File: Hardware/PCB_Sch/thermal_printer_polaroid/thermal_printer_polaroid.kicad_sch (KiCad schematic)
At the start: 45 parts, among them J2 USB4085-GF-A, SW0 SW_UP, SW1 SW_CAPTURE, SW2 SW_LEFT, SW3 SW_RIGHT, SW4 SW_DOWN, U1 TM4C123GH6PMI, U2 ov7670_module, U3 thermal_printer, U4 ST7735_LCD, U5 ESP8266_BREAKOUT, U6 UCC381DP-5G4, Y1 8 pF, 16 MHz

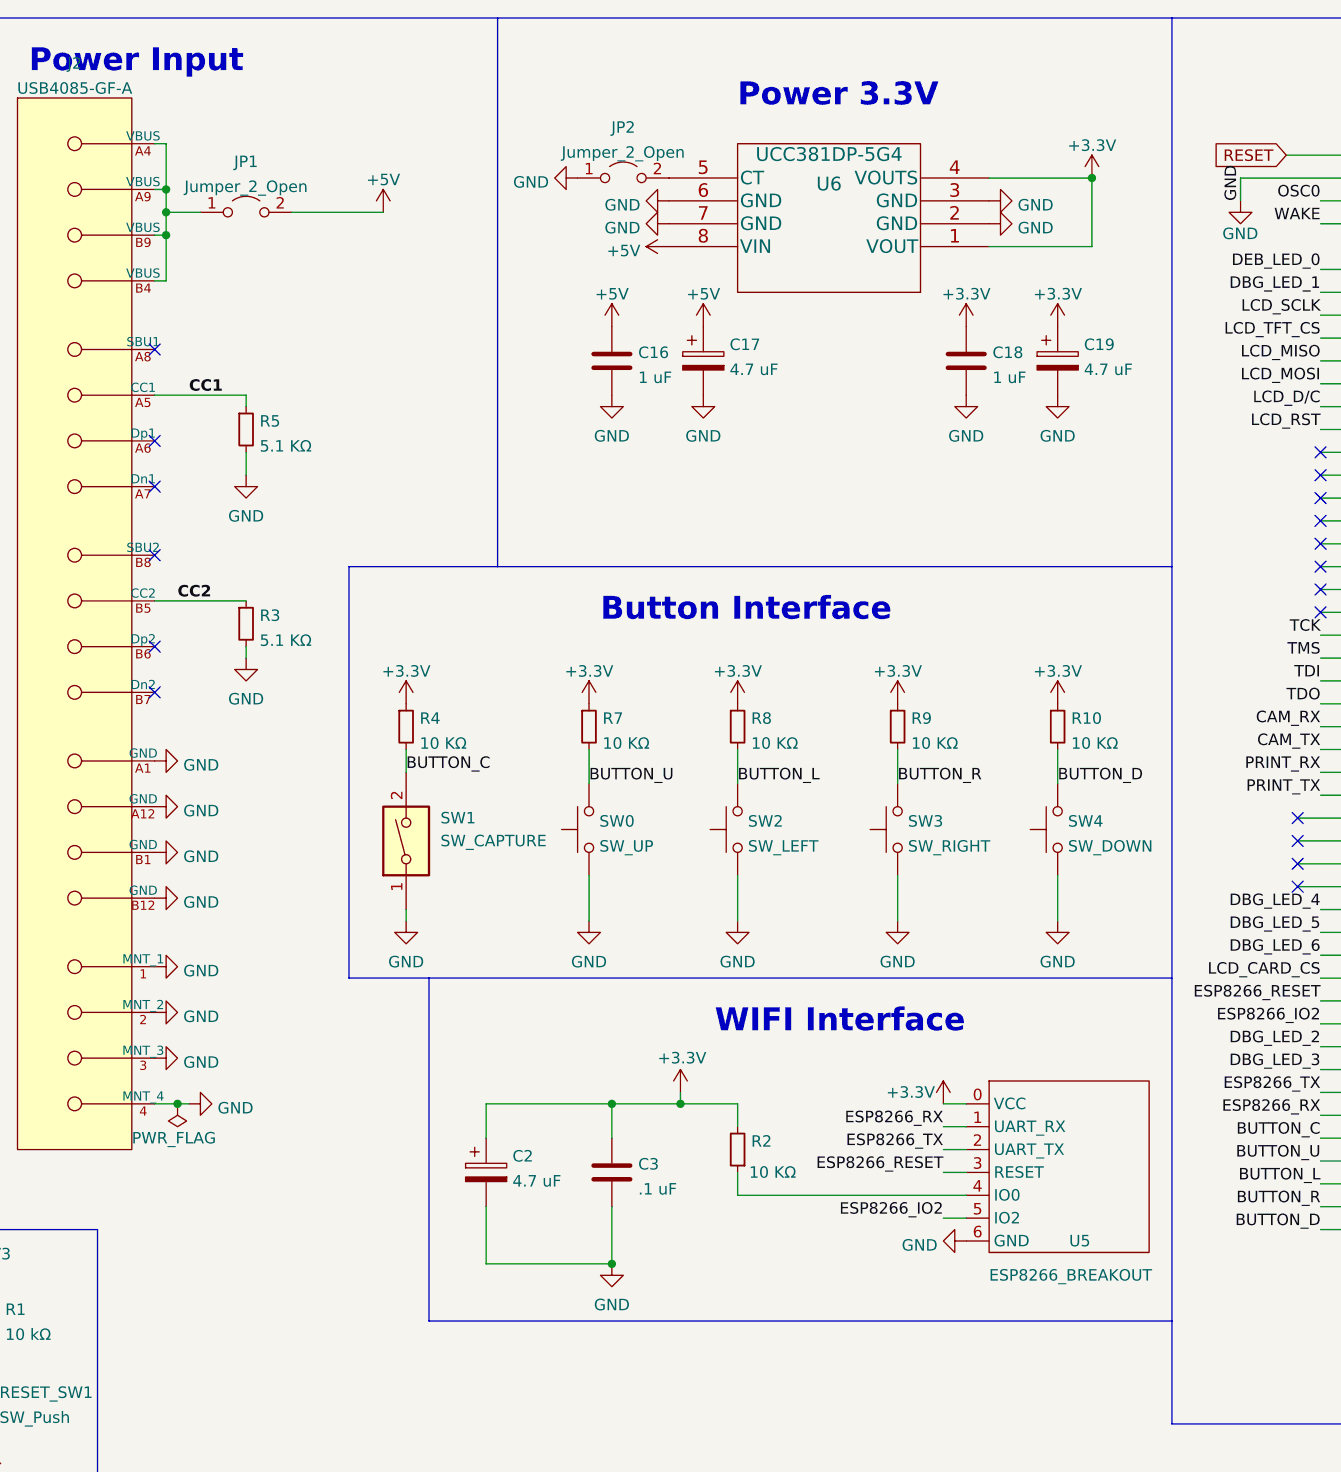
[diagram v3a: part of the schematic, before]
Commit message: Initial version of schematic done, all footprints assigned, need to review later before PCB start
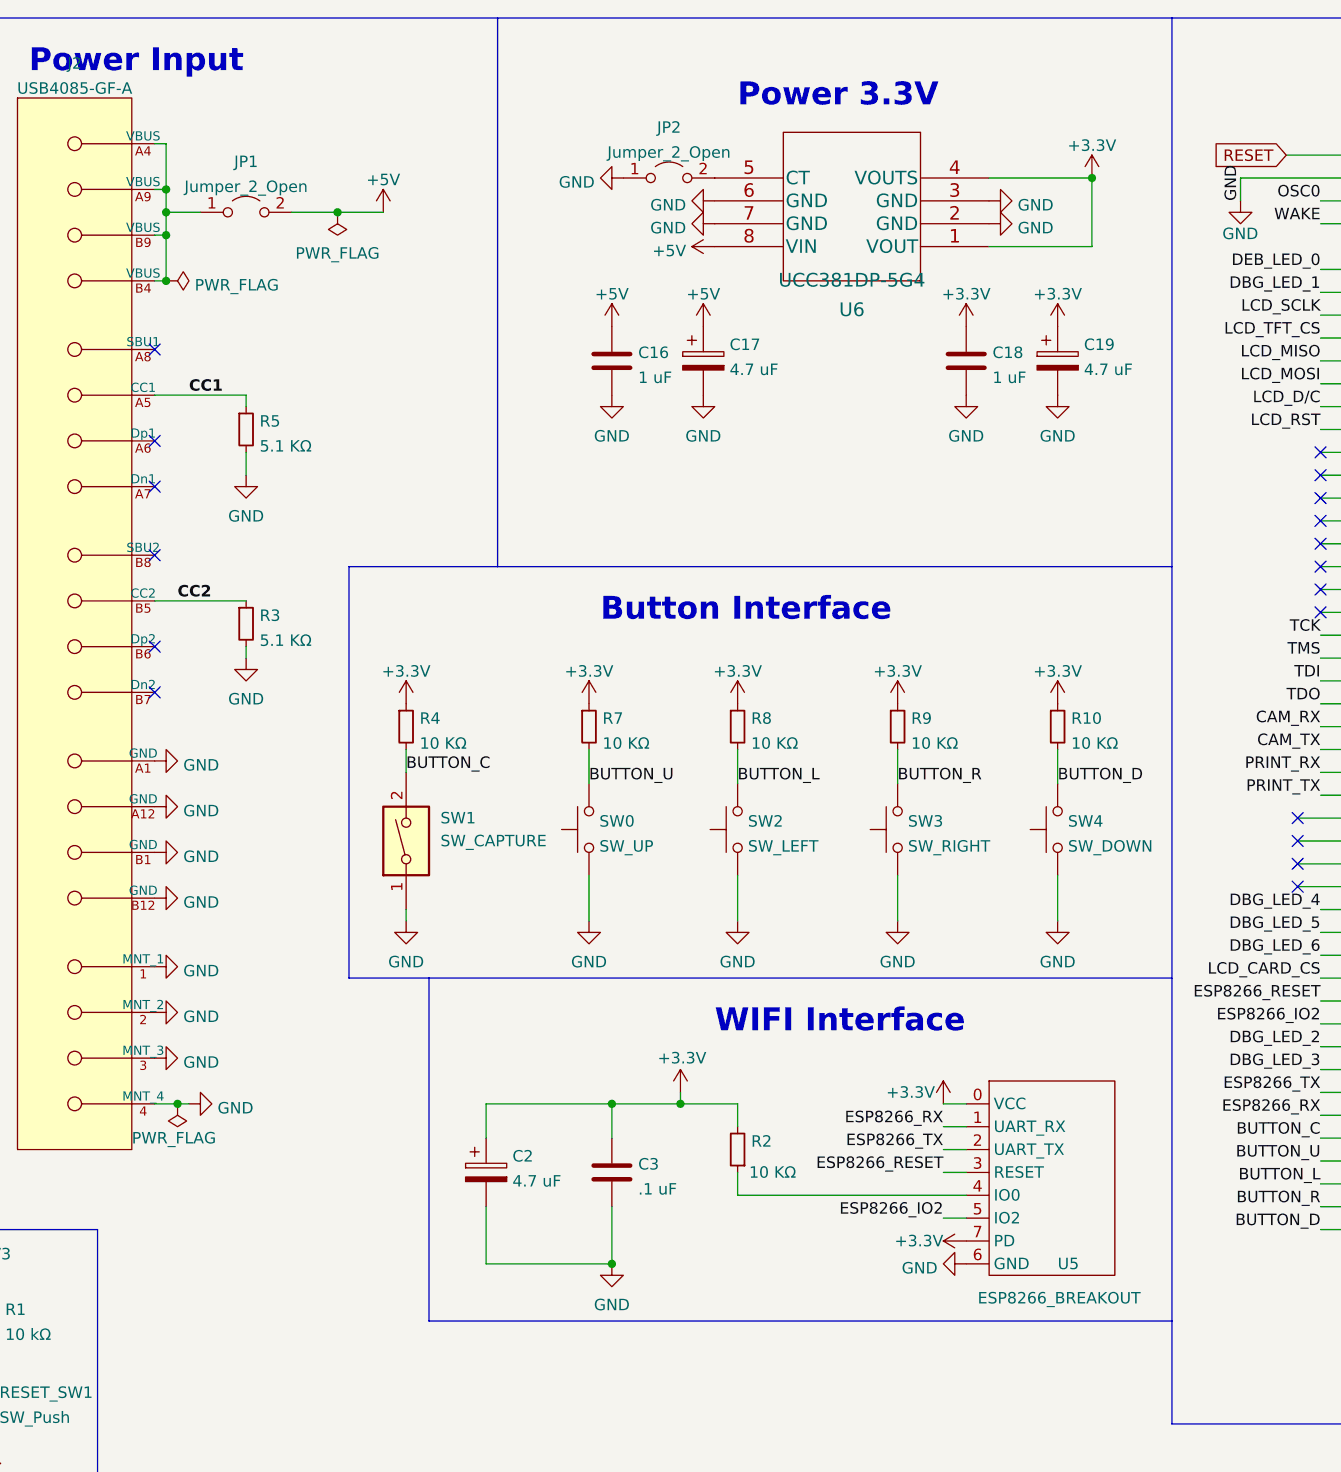
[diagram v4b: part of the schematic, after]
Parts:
- RESET_SW1: footprint Connector_PinHeader_2.54mm:PinHeader_1x02_P2.54mm_Vertical -> Button_Switch_SMD:SW_Push_1P1T_NO_6x6mm_H9.5mm
- SW0, SW2, SW3, SW4: footprint (none) -> Button_Switch_SMD:SW_Push_1P1T_NO_6x6mm_H9.5mm
- SW1: footprint (none) -> Connector_PinHeader_2.54mm:PinHeader_1x02_P2.54mm_Vertical
- U1: footprint QFP50P1200X1200X160-64N -> pcb_lib:QFP50P1200X1200X160-64N
- U5: footprint (none) -> Connector_PinHeader_2.54mm:PinHeader_2x04_P2.54mm_Vertical
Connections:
- net +3V3: now also U5.7 (PD)
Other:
- moved on the sheet: JP2, U6
